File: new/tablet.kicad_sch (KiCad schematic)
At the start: 12 parts, among them J1 Conn_02x20_Odd_Even, J2 USB_B_Micro, J3 Conn_02x04_Odd_Even, J4 Conn_02x04_Odd_Even, U1 STM32F429Z_E-G_Tx

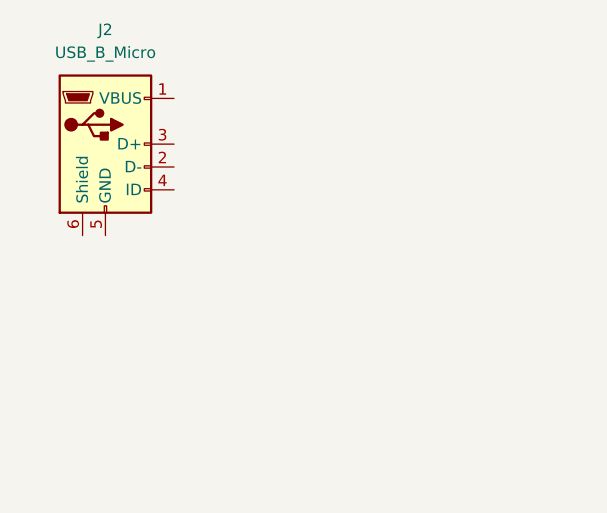
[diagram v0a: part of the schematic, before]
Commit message: add usb connector
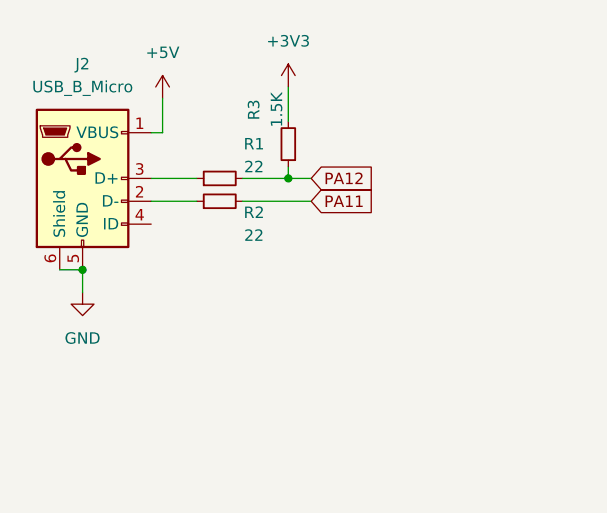
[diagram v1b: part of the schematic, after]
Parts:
- added R1, R2: 22, symbol Device:R_Small
- added R3: 1.5K, symbol Device:R_Small
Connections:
- net +3V3: now also R3.2
- net GND: now also J2.5 (GND), J2.6 (Shield)
- net +5V: now reaches J2.1 (VBUS)
- net at J2.2 (D-): now also R2.1
- net at J2.3 (D+): now also R1.1
- new net PA11: R2.2
- new net PA12: R1.2, R3.1
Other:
- moved on the sheet: J2
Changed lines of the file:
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@@
   (junction (at 104.14 52.07) (diameter 0) (color 0 0 0 0)
   )
+  (junction (at 45.72 31.75) (diameter 0) (color 0 0 0 0)
+  )
   (junction (at 101.6 67.31) (diameter 0) (color 0 0 0 0)
   )
@@
   (junction (at 109.22 259.08) (diameter 0) (color 0 0 0 0)
   )
+  (junction (at 22.86 41.91) (diameter 0) (color 0 0 0 0)
+  )
   (junction (at 116.84 67.31) (diameter 0) (color 0 0 0 0)
   )
@@
     (stroke (width 0) (type default))
   )
+  (wire (pts (xy 45.72 21.59) (xy 45.72 25.4))
+    (stroke (width 0) (type default))
+  )
   (wire (pts (xy 116.84 57.15) (xy 123.19 57.15))
     (stroke (width 0) (type default))
@@
     (stroke (width 0) (type default))
   )
+  (wire (pts (xy 31.75 22.86) (xy 31.75 26.67))
+    (stroke (width 0) (type default))
+  )
   (wire (pts (xy 116.84 67.31) (xy 116.84 72.39))
     (stroke (width 0) (type default))
@@
     (stroke (width 0) (type default))
   )
+  (wire (pts (xy 30.48 34.29) (xy 35.56 34.29))
+    (stroke (width 0) (type default))
+  )
   (wire (pts (xy 99.06 67.31) (xy 101.6 67.31))
     (stroke (width 0) (type default))
   )
+  (wire (pts (xy 22.86 44.45) (xy 22.86 41.91))
+    (stroke (width 0) (type default))
+  )
   (wire (pts (xy 121.92 67.31) (xy 121.92 72.39))
     (stroke (width 0) (type default))
@@
     (stroke (width 0) (type default))
   )
+  (wire (pts (xy 45.72 31.75) (xy 48.26 31.75))
+    (stroke (width 0) (type default))
+  )
   (wire (pts (xy 96.52 72.39) (xy 96.52 67.31))
     (stroke (width 0) (type default))
   )
+  (wire (pts (xy 20.32 41.91) (xy 22.86 41.91))
+    (stroke (width 0) (type default))
+  )
+  (wire (pts (xy 40.64 31.75) (xy 45.72 31.75))
+    (stroke (width 0) (type default))
+  )
   (wire (pts (xy 132.08 52.07) (xy 137.16 52.07))
     (stroke (width 0) (type default))
@@
     (stroke (width 0) (type default))
   )
+  (wire (pts (xy 45.72 31.75) (xy 45.72 30.48))
+    (stroke (width 0) (type default))
+  )
   (wire (pts (xy 97.79 57.15) (xy 104.14 57.15))
     (stroke (width 0) (type default))
@@
     (stroke (width 0) (type default))
   )
+  (wire (pts (xy 30.48 31.75) (xy 35.56 31.75))
+    (stroke (width 0) (type default))
+  )
   (wire (pts (xy 104.14 52.07) (xy 110.49 52.07))
     (stroke (width 0) (type default))
@@
     (stroke (width 0) (type default))
   )
+  (wire (pts (xy 40.64 34.29) (xy 48.26 34.29))
+    (stroke (width 0) (type default))
+  )
   (wire (pts (xy 114.3 67.31) (xy 116.84 67.31))
     (stroke (width 0) (type default))
@@
     (stroke (width 0) (type default))
   )
+  (wire (pts (xy 30.48 26.67) (xy 31.75 26.67))
+    (stroke (width 0) (type default))
+  )
   (wire (pts (xy 99.06 67.31) (xy 99.06 72.39))
     (stroke (width 0) (type default))
@@
   (wire (pts (xy 116.84 67.31) (xy 119.38 67.31))
     (stroke (width 0) (type default))
+  )
+  (global_label "PA11" (shape input) (at 48.26 34.29 0) (fields_autoplaced)
+    (effects (font (size 1.27 1.27)) (justify left))
+    (property "Intersheetrefs" "${INTERSHEET_REFS}" (at 56.0228 34.29 0)
+      (effects (font (size 1.27 1.27)) (justify left) hide)
+    )
+  )
+  (global_label "PA12" (shape input) (at 48.26 31.75 0) (fields_autoplaced)
+    (effects (font (size 1.27 1.27)) (justify left))
+    (property "Intersheetrefs" "${INTERSHEET_REFS}" (at 56.0228 31.75 0)
+      (effects (font (size 1.27 1.27)) (justify left) hide)
+    )
+  )
+  (symbol (lib_id "power:GND") (at 22.86 44.45 0) (unit 1)
+    (in_bom yes) (on_board yes) (dnp no) (fields_autoplaced)
+    (property "Reference" "#PWR06" (at 22.86 50.8 0)
+      (effects (font (size 1.27 1.27)) hide)
+    )
+    (property "Value" "GND" (at 22.86 49.53 0)
+      (effects (font (size 1.27 1.27)))
+    )
+    (property "Footprint" "" (at 22.86 44.45 0)
+      (effects (font (size 1.27 1.27)) hide)
+    )
+    (property "Datasheet" "" (at 22.86 44.45 0)
+      (effects (font (size 1.27 1.27)) hide)
+    )
+    (pin "1")
+    (instances
+      (project "tablet"
+        (path "/868516f5-1ea3-47ae-b277-3f67998564bb"
+          (reference "#PWR06") (unit 1)
+        )
+      )
+    )
   )
   (symbol (lib_id "Device:C_Small") (at 129.54 54.61 0) (unit 1)
@@
     )
   )
+  (symbol (lib_id "Device:R_Small") (at 38.1 31.75 90) (unit 1)
+    (in_bom yes) (on_board yes) (dnp no)
+    (property "Reference" "R1" (at 41.91 27.94 90)
+      (effects (font (size 1.27 1.27)))
+    )
+    (property "Value" "22" (at 41.91 30.48 90)
+      (effects (font (size 1.27 1.27)))
+    )
+    (property "Footprint" "" (at 38.1 31.75 0)
+      (effects (font (size 1.27 1.27)) hide)
+    )
+    (property "Datasheet" "~" (at 38.1 31.75 0)
+      (effects (font (size 1.27 1.27)) hide)
+    )
+    (pin "1")
+    (pin "2")
+    (instances
+      (project "tablet"
+        (path "/868516f5-1ea3-47ae-b277-3f67998564bb"
+          (reference "R1") (unit 1)
+        )
+      )
+    )
+  )
+  (symbol (lib_id "Device:R_Small") (at 45.72 27.94 180) (unit 1)
+    (in_bom yes) (on_board yes) (dnp no)
+    (property "Reference" "R3" (at 41.91 24.13 90)
+      (effects (font (size 1.27 1.27)))
+    )
+    (property "Value" "1.5K" (at 44.45 24.13 90)
+      (effects (font (size 1.27 1.27)))
+    )
+    (property "Footprint" "" (at 45.72 27.94 0)
+      (effects (font (size 1.27 1.27)) hide)
+    )
+    (property "Datasheet" "~" (at 45.72 27.94 0)
+      (effects (font (size 1.27 1.27)) hide)
+    )
+    (pin "1")
+    (pin "2")
+    (instances
+      (project "tablet"
+        (path "/868516f5-1ea3-47ae-b277-3f67998564bb"
+          (reference "R3") (unit 1)
+        )
+      )
+    )
+  )
   (symbol (lib_id "power:+3V3") (at 137.16 52.07 0) (unit 1)
     (in_bom yes) (on_board yes) (dnp no) (fields_autoplaced)
@@
     )
   )
-  (symbol (lib_id "Connector:USB_B_Micro") (at 25.4 27.94 0) (unit 1)
-    (in_bom yes) (on_board yes) (dnp no) (fields_autoplaced)
-    (property "Reference" "J2" (at 25.4 15.24 0)
-      (effects (font (size 1.27 1.27)))
-    )
-    (property "Value" "USB_B_Micro" (at 25.4 17.78 0)
-      (effects (font (size 1.27 1.27)))
-    )
-    (property "Footprint" "" (at 29.21 29.21 0)
-      (effects (font (size 1.27 1.27)) hide)
-    )
-    (property "Datasheet" "~" (at 29.21 29.21 0)
+  (symbol (lib_id "power:+5V") (at 31.75 22.86 0) (unit 1)
+    (in_bom yes) (on_board yes) (dnp no) (fields_autoplaced)
+    (property "Reference" "#PWR04" (at 31.75 26.67 0)
+      (effects (font (size 1.27 1.27)) hide)
+    )
+    (property "Value" "+5V" (at 31.75 17.78 0)
+      (effects (font (size 1.27 1.27)))
+    )
+    (property "Footprint" "" (at 31.75 22.86 0)
+      (effects (font (size 1.27 1.27)) hide)
+    )
+    (property "Datasheet" "" (at 31.75 22.86 0)
+      (effects (font (size 1.27 1.27)) hide)
+    )
+    (pin "1")
+    (instances
+      (project "tablet"
+        (path "/868516f5-1ea3-47ae-b277-3f67998564bb"
+          (reference "#PWR04") (unit 1)
+        )
+      )
+    )
+  )
+  (symbol (lib_id "Device:R_Small") (at 38.1 34.29 90) (unit 1)
+    (in_bom yes) (on_board yes) (dnp no)
+    (property "Reference" "R2" (at 41.91 35.56 90)
+      (effects (font (size 1.27 1.27)))
+    )
+    (property "Value" "22" (at 41.91 38.1 90)
+      (effects (font (size 1.27 1.27)))
+    )
+    (property "Footprint" "" (at 38.1 34.29 0)
+      (effects (font (size 1.27 1.27)) hide)
+    )
+    (property "Datasheet" "~" (at 38.1 34.29 0)
+      (effects (font (size 1.27 1.27)) hide)
+    )
+    (pin "1")
+    (pin "2")
+    (instances
+      (project "tablet"
+        (path "/868516f5-1ea3-47ae-b277-3f67998564bb"
+          (reference "R2") (unit 1)
+        )
+      )
+    )
+  )
+  (symbol (lib_id "Connector:USB_B_Micro") (at 22.86 31.75 0) (unit 1)
+    (in_bom yes) (on_board yes) (dnp no) (fields_autoplaced)
+    (property "Reference" "J2" (at 22.86 19.05 0)
+      (effects (font (size 1.27 1.27)))
+    )
+    (property "Value" "USB_B_Micro" (at 22.86 21.59 0)
+      (effects (font (size 1.27 1.27)))
+    )
+    (property "Footprint" "" (at 26.67 33.02 0)
+      (effects (font (size 1.27 1.27)) hide)
+    )
+    (property "Datasheet" "~" (at 26.67 33.02 0)
       (effects (font (size 1.27 1.27)) hide)
     )
@@
         )
       )
+    )
+  )
+  (symbol (lib_id "power:+3V3") (at 45.72 21.59 0) (unit 1)
+    (in_bom yes) (on_board yes) (dnp no) (fields_autoplaced)
+    (property "Reference" "#PWR05" (at 45.72 25.4 0)
+      (effects (font (size 1.27 1.27)) hide)
+    )
+    (property "Value" "+3V3" (at 45.72 16.51 0)
+      (effects (font (size 1.27 1.27)))
+    )
+    (property "Footprint" "" (at 45.72 21.59 0)
+      (effects (font (size 1.27 1.27)) hide)
+    )
+    (property "Datasheet" "" (at 45.72 21.59 0)
+      (effects (font (size 1.27 1.27)) hide)
+    )
+    (pin "1")
+    (instances
+      (project "tablet"
+        (path "/868516f5-1ea3-47ae-b277-3f67998564bb"
+          (reference "#PWR05") (unit 1)
+        )
+      )

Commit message: add footprints
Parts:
- BT1: footprint (none) -> Battery:BatteryHolder_Keystone_3000_1x12mm
- C1, C2, C3, C4, C5, C6: footprint (none) -> Capacitor_SMD:C_0603_1608Metric
- J1: footprint (none) -> Connector_PinHeader_2.00mm:PinHeader_2x20_P2.00mm_Vertical
- J2: footprint (none) -> Connector_USB:USB_Micro-B_Molex-105017-0001
- J3, J4: footprint (none) -> Connector_PinHeader_2.54mm:PinHeader_2x04_P2.54mm_Vertical
- R1, R2, R3: footprint (none) -> Resistor_SMD:R_0603_1608Metric
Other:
- note added: "USB CONNECTOR"
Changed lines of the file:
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@@
     (stroke (width 0) (type default))
+  )
+  (rectangle (start 12.7 12.7) (end 60.96 53.34)
+    (stroke (width 0) (type default))
+    (fill (type none))
+  )
+  (text "USB CONNECTOR" (at 12.7 15.24 0)
+    (effects (font (size 1.27 1.27)) (justify left bottom))
   )
   (global_label "PA11" (shape input) (at 48.26 34.29 0) (fields_autoplaced)
@@
       (effects (font (size 1.27 1.27)) (justify left))
     )
-    (property "Footprint" "" (at 129.54 54.61 0)
+    (property "Footprint" "Capacitor_SMD:C_0603_1608Metric" (at 129.54 54.61 0)
       (effects (font (size 1.27 1.27)) hide)
     )
@@
       (effects (font (size 1.27 1.27)) (justify left))
     )
-    (property "Footprint" "" (at 104.14 54.61 0)
+    (property "Footprint" "Capacitor_SMD:C_0603_1608Metric" (at 104.14 54.61 0)
       (effects (font (size 1.27 1.27)) hide)
     )
@@
       (effects (font (size 1.27 1.27)))
     )
-    (property "Footprint" "" (at 236.22 120.65 0)
+    (property "Footprint" "Connector_PinHeader_2.54mm:PinHeader_2x04_P2.54mm_Vertical" (at 236.22 120.65 0)
       (effects (font (size 1.27 1.27)) hide)
     )
@@
       (effects (font (size 1.27 1.27)))
     )
-    (property "Footprint" "" (at 236.22 99.06 0)
+    (property "Footprint" "Connector_PinHeader_2.54mm:PinHeader_2x04_P2.54mm_Vertical" (at 236.22 99.06 0)
       (effects (font (size 1.27 1.27)) hide)
     )
@@
       (effects (font (size 1.27 1.27)))
     )
-    (property "Footprint" "" (at 38.1 31.75 0)
+    (property "Footprint" "Resistor_SMD:R_0603_1608Metric" (at 38.1 31.75 0)
       (effects (font (size 1.27 1.27)) hide)
     )
@@
   (symbol (lib_id "Device:R_Small") (at 45.72 27.94 180) (unit 1)
     (in_bom yes) (on_board yes) (dnp no)
-    (property "Reference" "R3" (at 41.91 24.13 90)
-      (effects (font (size 1.27 1.27)))
-    )
-    (property "Value" "1.5K" (at 44.45 24.13 90)
-      (effects (font (size 1.27 1.27)))
-    )
-    (property "Footprint" "" (at 45.72 27.94 0)
+    (property "Reference" "R3" (at 50.3404 27.6502 90)
+      (effects (font (size 1.27 1.27)))
+    )
+    (property "Value" "1.5K" (at 48.26 26.67 90)
+      (effects (font (size 1.27 1.27)))
+    )
+    (property "Footprint" "Resistor_SMD:R_0603_1608Metric" (at 45.72 27.94 0)
       (effects (font (size 1.27 1.27)) hide)
     )
@@
       (effects (font (size 1.27 1.27)) (justify left))
     )
-    (property "Footprint" "" (at 116.84 54.61 0)
+    (property "Footprint" "Capacitor_SMD:C_0603_1608Metric" (at 116.84 54.61 0)
       (effects (font (size 1.27 1.27)) hide)
     )
@@
       (effects (font (size 1.27 1.27)))
     )
-    (property "Footprint" "" (at 38.1 34.29 0)
+    (property "Footprint" "Resistor_SMD:R_0603_1608Metric" (at 38.1 34.29 0)
       (effects (font (size 1.27 1.27)) hide)
     )
@@
       (effects (font (size 1.27 1.27)))
     )
-    (property "Footprint" "" (at 26.67 33.02 0)
+    (property "Footprint" "Connector_USB:USB_Micro-B_Molex-105017-0001" (at 26.67 33.02 0)
       (effects (font (size 1.27 1.27)) hide)
     )
@@
       (effects (font (size 1.27 1.27)) (justify left))
     )
-    (property "Footprint" "" (at 97.79 54.61 0)
+    (property "Footprint" "Capacitor_SMD:C_0603_1608Metric" (at 97.79 54.61 0)
       (effects (font (size 1.27 1.27)) hide)
     )
@@
       (effects (font (size 1.27 1.27)) (justify left))
     )
-    (property "Footprint" "" (at 123.19 54.61 0)
+    (property "Footprint" "Capacitor_SMD:C_0603_1608Metric" (at 123.19 54.61 0)
       (effects (font (size 1.27 1.27)) hide)
     )
@@
       (effects (font (size 1.27 1.27)) (justify left))
     )
-    (property "Footprint" "" (at 110.49 54.61 0)
+    (property "Footprint" "Capacitor_SMD:C_0603_1608Metric" (at 110.49 54.61 0)
       (effects (font (size 1.27 1.27)) hide)
     )
@@
       (effects (font (size 1.27 1.27)))
     )
-    (property "Footprint" "" (at 236.22 53.34 0)
+    (property "Footprint" "Connector_PinHeader_2.00mm:PinHeader_2x20_P2.00mm_Vertical" (at 236.22 53.34 0)
       (effects (font (size 1.27 1.27)) hide)
     )
@@
       (effects (font (size 1.27 1.27)) (justify right))
     )
-    (property "Footprint" "" (at 93.98 63.754 90)
-      (effects (font (size 1.27 1.27)) hide)
-    )
+    (property "Footprint" "Battery:BatteryHolder_Keystone_3000_1x12mm" (at 93.98 63.754 90)
+      (effects (font (size 1.27 1.27)) hide)
+    )

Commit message: place header on pcb
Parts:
- J1: footprint Connector_PinHeader_2.00mm:PinHeader_2x20_P2.00mm_Vertical -> Connector_PinHeader_2.54mm:PinHeader_2x20_P2.54mm_Vertical
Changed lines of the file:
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@@
       (effects (font (size 1.27 1.27)))
     )
-    (property "Footprint" "Connector_PinHeader_2.00mm:PinHeader_2x20_P2.00mm_Vertical" (at 236.22 53.34 0)
+    (property "Footprint" "Connector_PinHeader_2.54mm:PinHeader_2x20_P2.54mm_Vertical" (at 236.22 53.34 0)
       (effects (font (size 1.27 1.27)) hide)
     )

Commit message: wiring screen + sdcard
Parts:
- added C7, C8: 2.2uF, Capacitor_SMD:C_0603_1608Metric, symbol Device:C_Small
- J1: value Conn_02x20_Odd_Even -> FSMC/TOUCH-SPI
- J3: value Conn_02x04_Odd_Even -> SD/CARD
- J4: value Conn_02x04_Odd_Even -> FLASH/FONT
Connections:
- net +3V3: now also J1.39 (Pin_39)
- net GND: now also J1.1 (Pin_1), J1.40 (Pin_40), J3.6 (Pin_6), C7.2, C8.2
- net PC11-DAT3: now reaches J3.1 (Pin_1)
- net PC11-DAT3: now also U1.112 (PC11)
- net PC10-DAT2: now reaches J3.2 (Pin_2)
- net PC10-DAT2: now also U1.111 (PC10)
- net PC12-CLK: now reaches J3.3 (Pin_3)
- net PC12-CLK: now also U1.113 (PC12)
- net PD2-CMD: now reaches J3.4 (Pin_4)
- net PD2-CMD: now also U1.116 (PD2)
- net PC8-DAT0: now reaches J3.5 (Pin_5)
- net PC8-DAT0: now also U1.98 (PC8)
- net PC0-SDDETECT: now reaches J3.7 (Pin_7)
- net PC0-SDDETECT: now also U1.26 (PC0)
- net PC9-DAT1: now reaches J3.8 (Pin_8)
- net PC9-DAT1: now also U1.99 (PC9)
- net PA10-BL: now reaches U1.102 (PA10)
- net PA10-BL: now also J1.2 (Pin_2)
- net at U1.106 (VCAP_2): now also C8.1
- net PD0-D2: now reaches U1.114 (PD0)
- net PD0-D2: now also J1.30 (Pin_30)
- net PD1-D3: now reaches U1.115 (PD1)
- net PD1-D3: now also J1.29 (Pin_29)
- net PD4-/RD: now reaches U1.118 (PD4)
- net PD4-/RD: now also J1.36 (Pin_36)
- net PD5-/WR: now reaches U1.119 (PD5)
- net PD5-/WR: now also J1.35 (Pin_35)
- net PD6-TP/IRQ: now reaches U1.122 (PD6)
- net PD6-TP/IRQ: now also J1.3 (Pin_3)
- net PD7-/CS: now reaches U1.123 (PD7)
- net PD7-/CS: now also J1.38 (Pin_38)
- net BOOT0: now reaches U1.138 (BOOT0)
- net BOOT1: now reaches U1.48 (PB2)
- net PE7-D4: now reaches U1.58 (PE7)
- net PE7-D4: now also J1.28 (Pin_28)
- net PE8-D5: now reaches U1.59 (PE8)
- net PE8-D5: now also J1.27 (Pin_27)
- net PE9-D6: now reaches U1.60 (PE9)
- net PE9-D6: now also J1.26 (Pin_26)
- net PE10-D7: now reaches U1.63 (PE10)
- net PE10-D7: now also J1.25 (Pin_25)
- net PE11-D8: now reaches U1.64 (PE11)
- net PE11-D8: now also J1.24 (Pin_24)
- net PE12-D9: now reaches U1.65 (PE12)
- net PE12-D9: now also J1.23 (Pin_23)
- net PE13-D10: now reaches U1.66 (PE13)
- net PE13-D10: now also J1.22 (Pin_22)
- net PE14-D11: now reaches U1.67 (PE14)
- net PE14-D11: now also J1.21 (Pin_21)
- net PE15-D12: now reaches U1.68 (PE15)
- net PE15-D12: now also J1.20 (Pin_20)
- net at U1.71 (VCAP_1): now also C7.1
- net PB12-TP/CS: now reaches U1.73 (PB12)
- net PB12-TP/CS: now also J1.8 (Pin_8)
- net PB13-TP/SCK: now reaches U1.74 (PB13)
- net PB13-TP/SCK: now also J1.7 (Pin_7)
- net PB14-SO: now reaches U1.75 (PB14)
- net PB14-SO: now also J1.5 (Pin_5)
- net PB15-SI: now reaches U1.76 (PB15)
- net PB15-SI: now also J1.6 (Pin_6)
- net PD8-D13: now reaches U1.77 (PD8)
- net PD8-D13: now also J1.19 (Pin_19)
- net PD9-D14: now reaches U1.78 (PD9)
- net PD9-D14: now also J1.18 (Pin_18)
- net PD10-D15: now reaches U1.79 (PD10)
- net PD10-D15: now also J1.17 (Pin_17)
- net PD11-RS: now reaches U1.80 (PD11)
- net PD11-RS: now also J1.37 (Pin_37)
- net PD14-D0: now reaches U1.85 (PD14)
- net PD14-D0: now also J1.32 (Pin_32)
- net PD15-D1: now reaches J1.31 (Pin_31)
- net TE: now reaches J1.33 (Pin_33)
- net TFT-RESET: now reaches J1.34 (Pin_34)
